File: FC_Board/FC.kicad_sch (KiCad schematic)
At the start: 31 parts, among them J1 Programmer_pins, Q1 PMOS, U1 PIC32MZ2048EFH100-I/PF, U2 LM7805MPX/NOPB, U3 LDL1117S33R

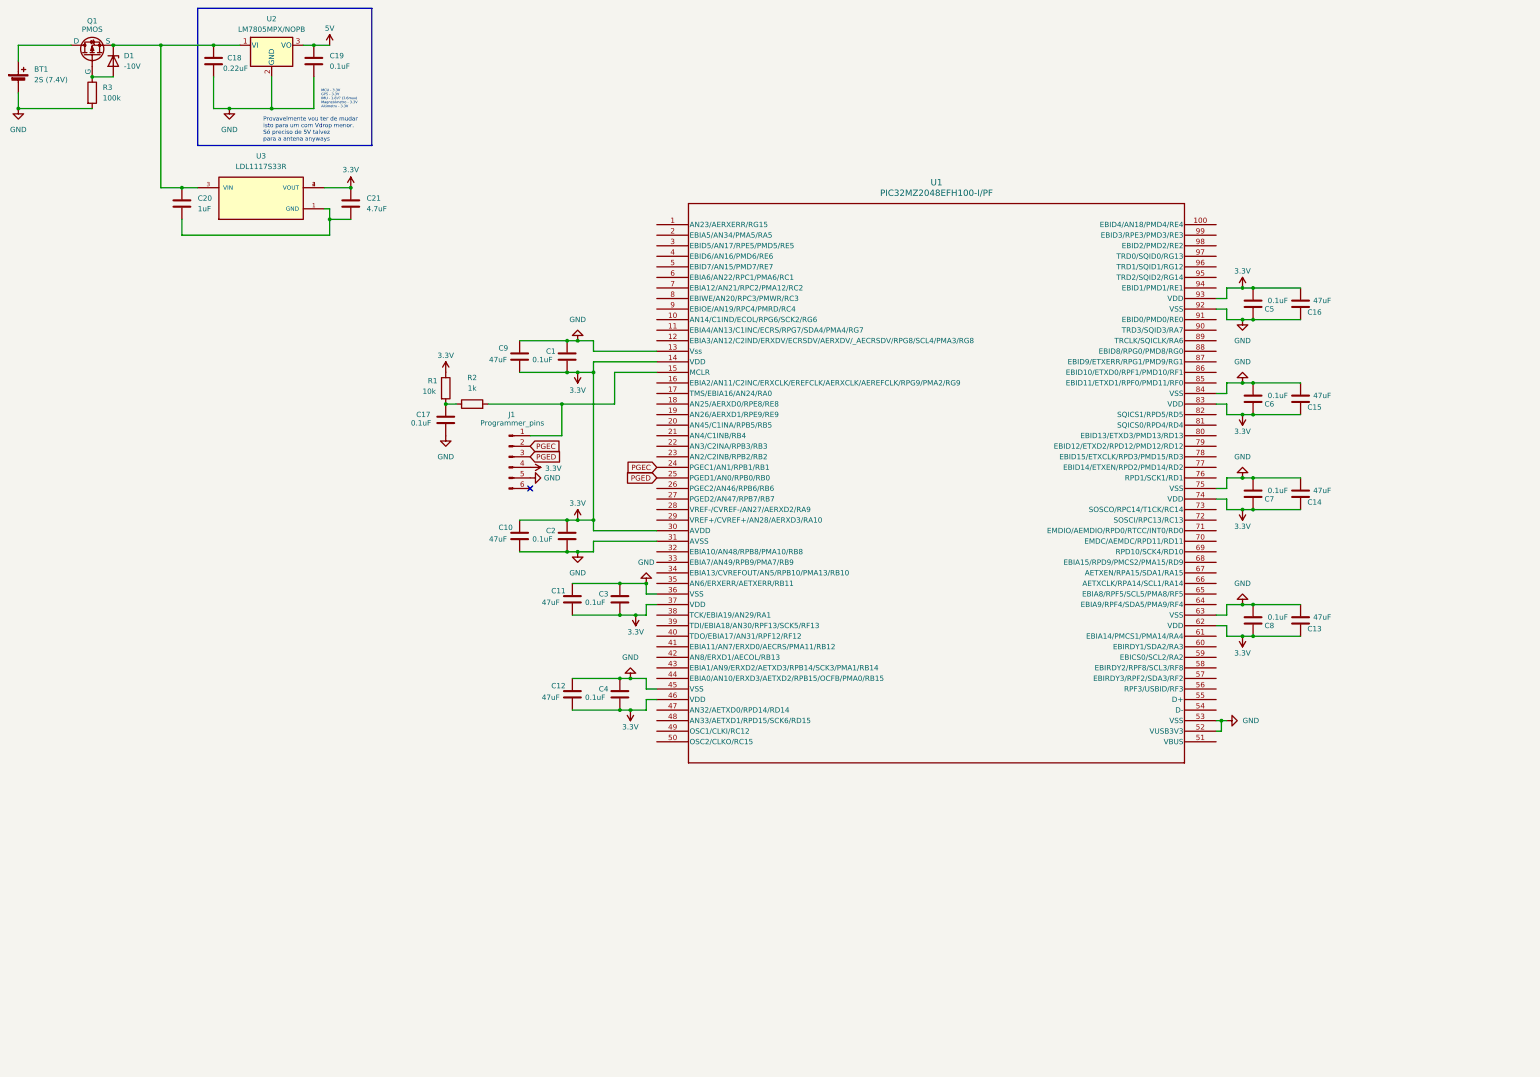
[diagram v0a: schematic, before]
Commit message: Added datasheets and footprints/symbols
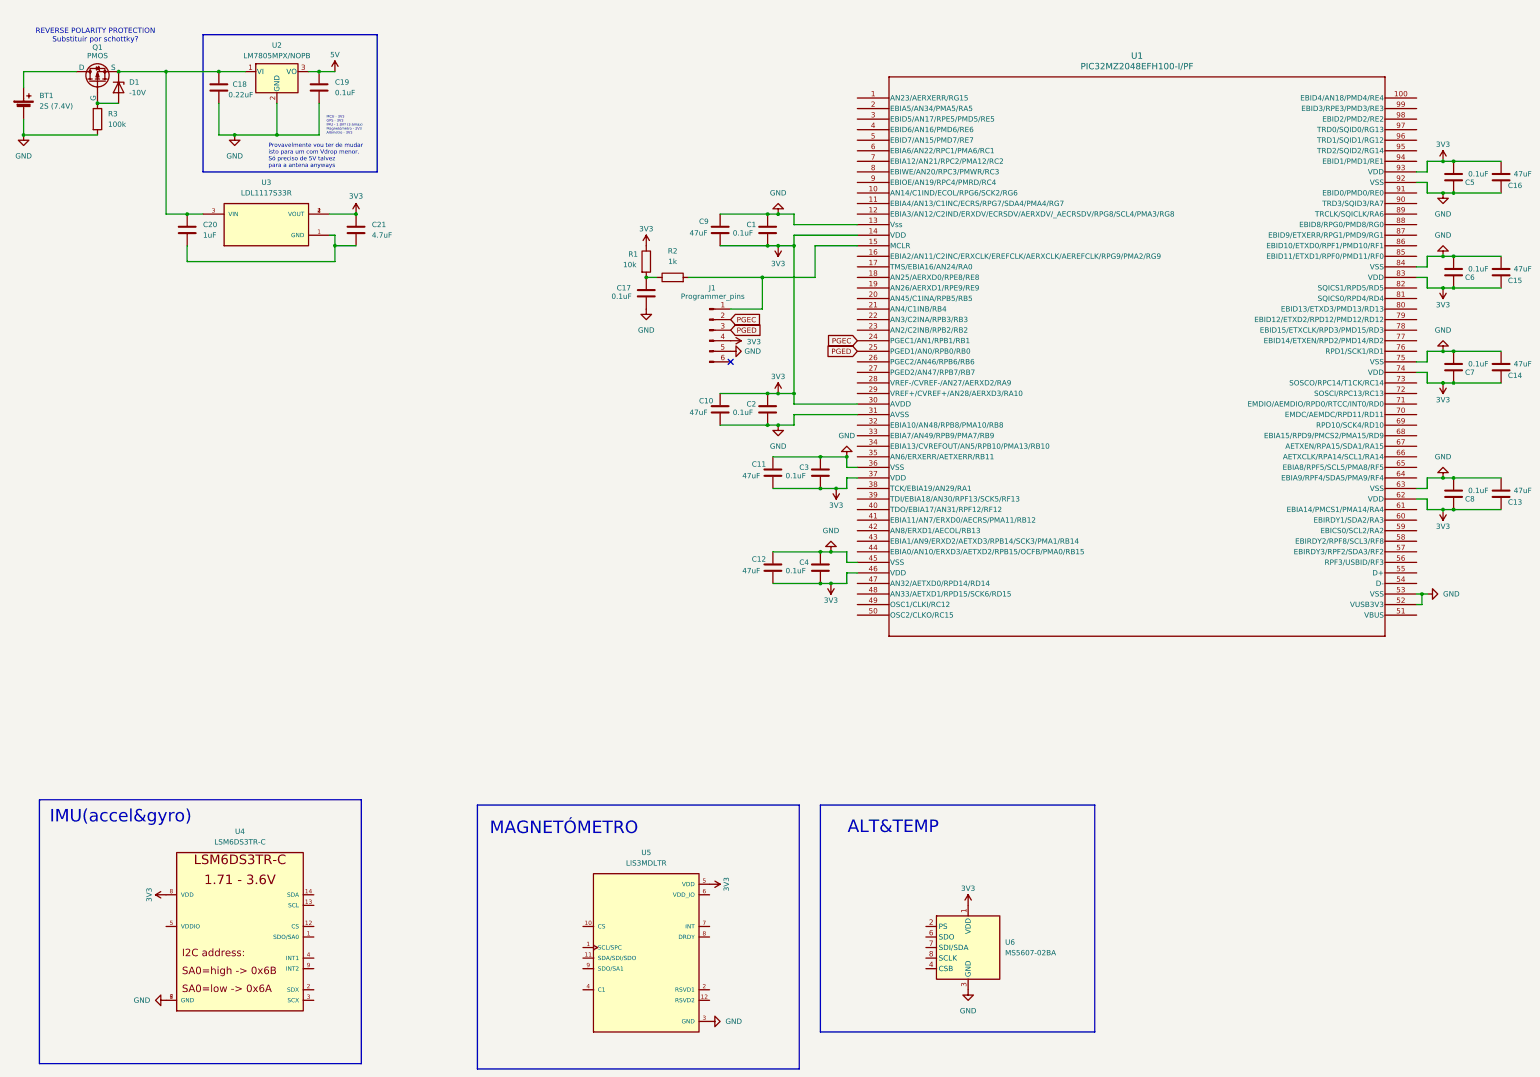
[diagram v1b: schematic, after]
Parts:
- added U4: LSM6DS3TR-C, LSM6DS3TR-C:LGA-14-2.5X3MM, symbol LSM6DS3TR-C:LSM6DS3TR-C
- added U5: LIS3MDLTR, LIS3MDLTR:XDCR_LIS3MDLTR, symbol LIS3MDLTR:LIS3MDLTR
- added U6: MS5607-02BA, Package_LGA:LGA-8_3x5mm_P1.25mm, symbol Sensor_Pressure:MS5607-02BA
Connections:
- net GND: now also U4.6 (GND), U4.7 (GND), U5.3 (GND), U6.3 (GND)
- net 3.3V renamed 3V3
- net 3V3: now also U4.8 (VDD), U5.5 (VDD), U6.1 (VDD)
- new net: U6.4 (CSB), U6.5 (CSB)
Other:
- note added: "ALT&TEMP"
- note added: "IMU(accel&gyro)"
- note added: "MAGNETÓMETRO"
- note added: "MCU - 3V3 GPS - 3V3 IMU - 1.8V? (3.6max) Magnetómetro - 3V3 Altímetro - 3V3"
- note added: "REVERSE POLARITY PROTECTION Substituir por schottky?"
- note removed: "MCU - 3.3V GPS - 3.3V IMU - 1.8V? (3.6max) Magnetómetro - 3.3V Altímetro - 3.3V"
- moved on the sheet: BT1, C1, C10, C11, C12, C13, C14, C15, C16, C17, C18, C19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

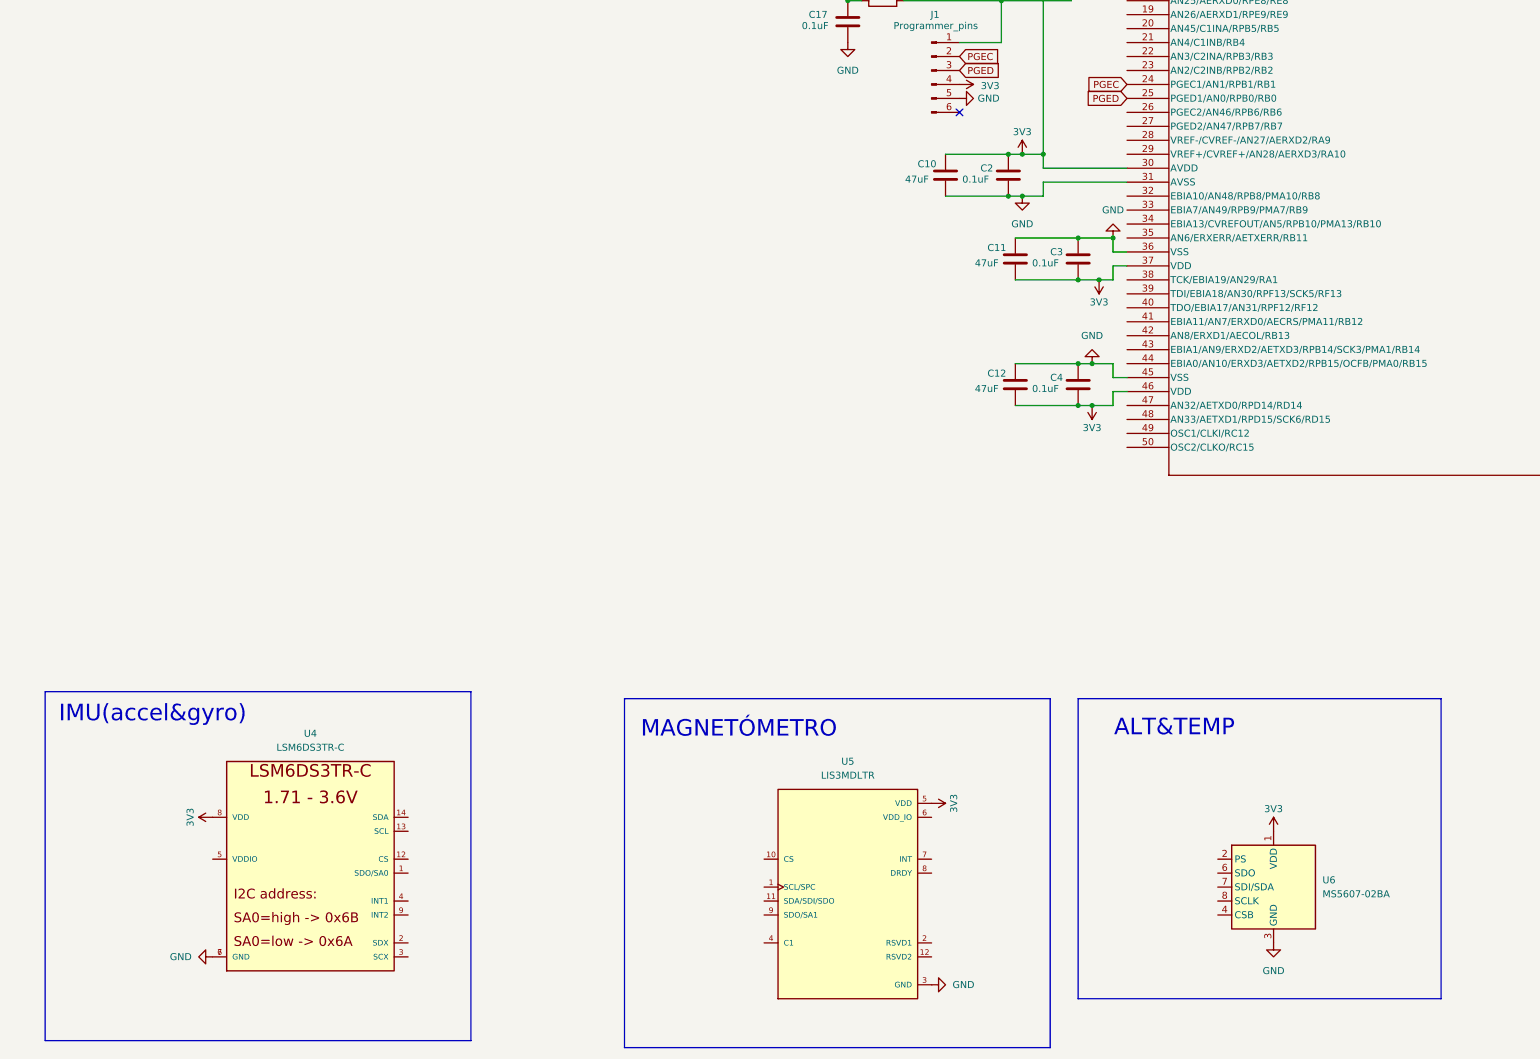
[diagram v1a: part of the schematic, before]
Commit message: Added IC decoupling and basic connections
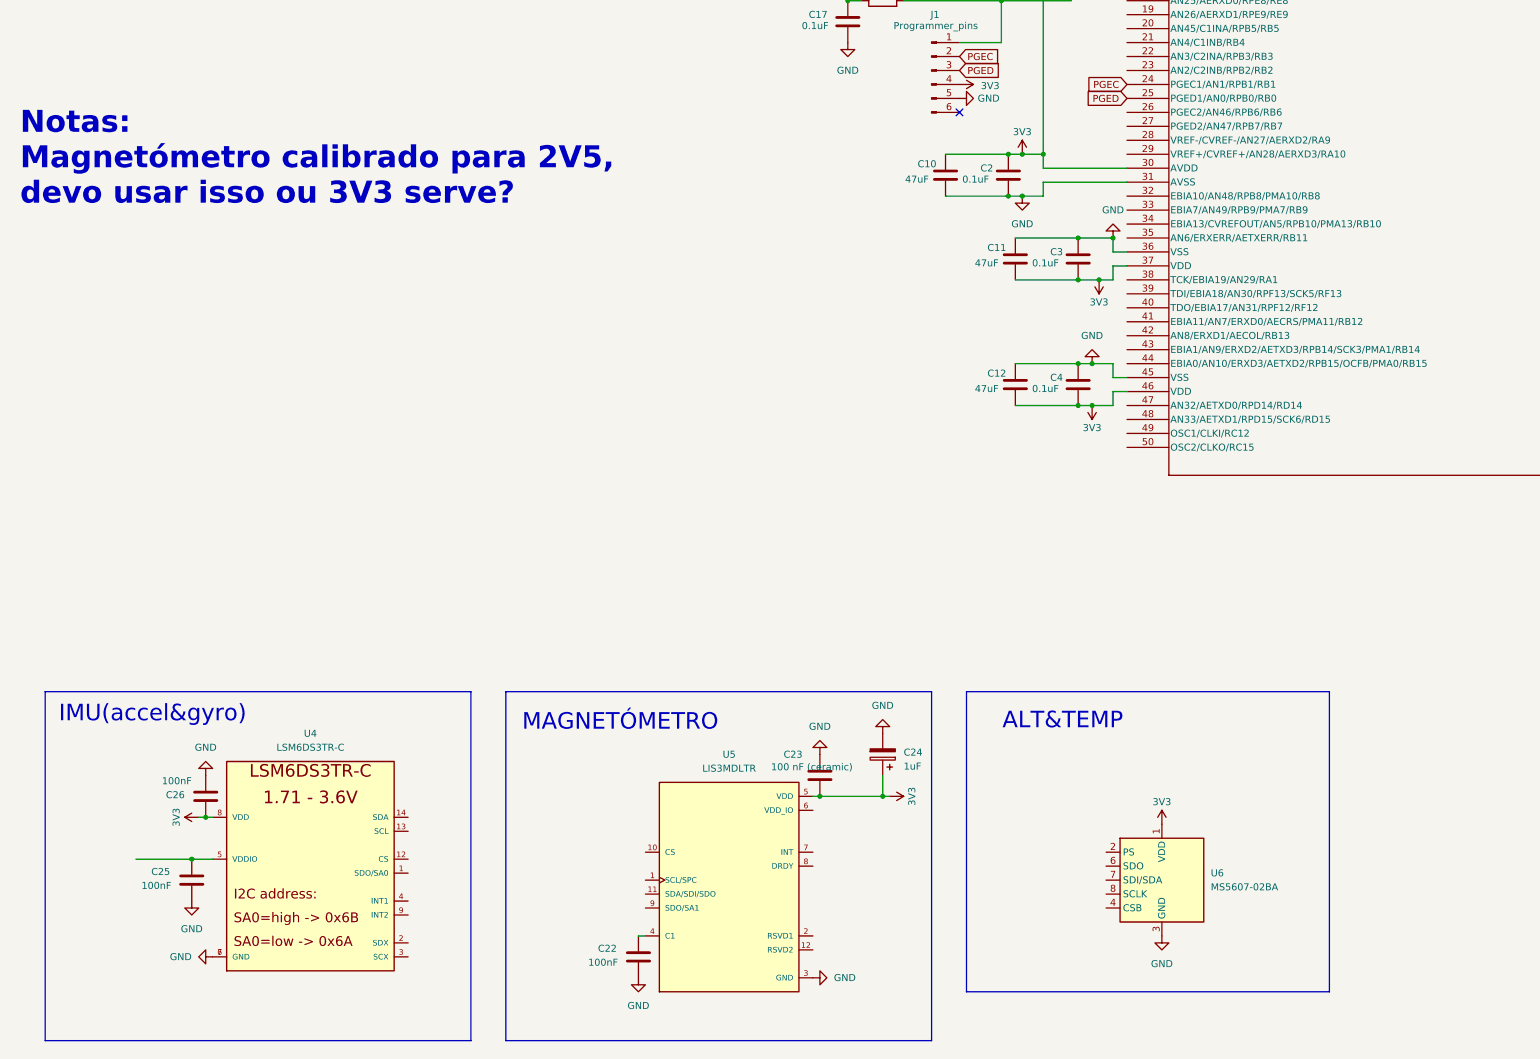
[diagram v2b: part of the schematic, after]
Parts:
- added C22, C25, C26: 100nF, symbol Device:C
- added C23: 100 nF (ceramic), symbol Device:C
- added C24: 1uF, symbol Device:C_Polarized
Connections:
- net 3V3: now also C23.2, C24.1, C26.1
- net GND: now also C22.2, C23.1, C24.2, C25.2, C26.2
- net at U4.5 (VDDIO): now also C25.1
- net at U5.4 (C1): now also C22.1
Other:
- note added: "Notas: Magnetómetro calibrado para 2V5, devo usar isso ou 3V3 serve?"
- moved on the sheet: U5, U6

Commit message: Schematic progress
GPS data logging, Power monitoring and other updates to schematic.
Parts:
- added AE1: Antenna, symbol Device:Antenna
- added BZ1: Buzzer, symbol Device:Buzzer
- added C27: 100 nF (ceramic), symbol Device:C
- added C28, C29, C30: 0.1uF, symbol Device:C
- added C31: C, symbol Device:C
- added D2: LED, symbol Device:LED
- added J2: Pyro1, symbol Connector:Conn_01x02_Pin
- added J3: Pyro2, symbol Connector:Conn_01x02_Pin
- added J4: Pyro3, symbol Connector:Conn_01x02_Pin
- added J5: Pyro4, symbol Connector:Conn_01x02_Pin
- added J6, J7: Conn_01x03, symbol Connector_Generic:Conn_01x03
- added M1, M2, M3, M4: Motor_Servo, symbol Motor:Motor_Servo
- added Q2, Q3, Q4, Q5: NMOS, symbol Simulation_SPICE:NMOS
- added R10, R7, R9: R, symbol Device:R
- added R4, R5, R6: 10k, symbol Device:R
- added R8: R_Shunt, symbol Device:R_Shunt
- added U7: NEO-M8Q, NEO-M8Q:XCVR_NEO-M8Q, symbol NEO-M8Q:NEO-M8Q
- added U8: SST26VF032BT-104I/SM, SOIJ8_SM_MCH, symbol 2025-01-11_19-47-35:SST26VF032BT-104I_SM
- added U9: INA219AxD, Package_SO:SOIC-8_3.9x4.9mm_P1.27mm, symbol Sensor_Energy:INA219AxD
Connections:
- net 3V3: now also C25.1, U4.5 (VDDIO), U5.6 (VDD_IO), C27.2, C28.1, C29.2, C30.2, J6.3 (Pin_3), J7.3 (Pin_3), R4.2, R5.2, R6.2, U7.22 (V_BCKP), U7.23 (VCC), U8.8 (VDD), U9.5 (VS)
- net GND: now also U4.2 (SDX), U4.3 (SCX), U5.12 (RSVD2), U5.2 (RSVD1), BZ1.2 (-), C27.1, C28.2, C29.1, C30.1, J6.1 (Pin_1), J7.1 (Pin_1), M1.3 (-), M2.3 (-), M3.3 (-), M4.3 (-), Q2.3 (S), Q3.3 (S), Q4.3 (S), Q5.3 (S), R7.1, U7.10 (GND), U7.12 (GND), U7.13 (GND), U7.24 (GND), U8.4 (VSS), U9.6 (GND)
- net IMU_SDO: now reaches U4.1 (SDO/SA0)
- net IMU_CS: now reaches U4.12 (CS)
- net IMU_CS: now also R6.1
- net IMU_CLK: now reaches U4.13 (SCL)
- net IMU_SDI: now reaches U4.14 (SDA)
- net at U6.2 (PS): now also J6.2 (Pin_2)
- net ALT_CS: now reaches U6.4 (CSB), U6.5 (CSB)
- net ALT_CS: now also R4.1
- net ALT_SDO: now reaches U6.6 (SDO)
- net ALT_SDI: now reaches U6.7 (SDI/SDA)
- net ALT_CLK: now reaches U6.8 (SCLK)
- net MAG_CLK: now reaches U5.1 (SCL/SPC)
- net MAG_CS: now reaches U5.10 (CS)
- net MAG_CS: now also R5.1
- net MAG_SDI: now reaches U5.11 (SDA/SDI/SDO)
- net MAG_SDO: now reaches U5.9 (SDO/SA1)
- net Battery_VDD: now reaches BT1.1 (+), Q1.1 (D)
- net Battery_VDD: now also J2.1 (Pin_1), J3.1 (Pin_1), J4.1 (Pin_1), J5.1 (Pin_1)
- new net: J2.2 (Pin_2), Q2.1 (D)
- new net: C31.2, R10.1, R8.3
- new net: R10.2, U9.7 (IN-)
- new net: J5.2 (Pin_2), Q5.1 (D)
- new net: R9.2, U9.8 (IN+)
- new net: J3.2 (Pin_2), Q3.1 (D)
- new net: J7.2 (Pin_2), U7.2 (D_SEL)
- new net: J4.2 (Pin_2), Q4.1 (D)
- new net: C31.1, R8.2, R9.1
- new net: D2.1 (K), R7.2
- new net: AE1.1 (A), U7.11 (RF_IN)
- new net Buzzer_pin: BZ1.1 (+), D2.2 (A)
- new net FLASH_CLK: U8.6 (SCK)
- new net FLASH_EN: U8.1 (CE#)
- new net GPS_CLK: U7.19 (SCL/SPI_CLK)
- new net GPS_CS: U7.18 (SDA/SPI_CS_N)
- new net GPS_INT: U7.4 (EXTINT)
- new net GPS_RESET: U7.8 (RESET_N)
- new net GPS_RXD: U7.21 (RXD/SPI_MOSI)
- new net GPS_TXD: U7.20 (TXD/SPI_MISO)
- new net PWR_SDA: U9.3 (SDA)
- new net PWR_SDL: U9.4 (SCL)
- new net Pyro_channel1: Q2.2 (G)
- new net Pyro_channel2: Q3.2 (G)
- new net Pyro_channel3: Q4.2 (G)
- new net Pyro_channel4: Q5.2 (G)
- new net SERVO_+: M1.2 (+), M2.2 (+), M3.2 (+), M4.2 (+)
- new net SERVO_1: M1.1 (PWM)
- new net SERVO_2: M2.1 (PWM)
- new net SERVO_3: M3.1 (PWM)
- new net SERVO_4: M4.1 (PWM)
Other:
- note added: "Active antenna only"
- note added: "Buzzer"
- note added: "Confirmar mais tarde ligações a pinos A0/A1"
- note added: "Convém confirmar se PIC consegue dar drive do buzzer e led simultaneamente, talvez fosse boa ideia usar open drain type config"
- note added: "De preferência ter este sinal num canal separado ao invés dum barramento. (ADC sensível / Recomendado no datasheet)"
- note added: "GPS"
- note added: "GPS FLASH DATA LOGGING"
- note added: "I2C"
- note added: "LNA EN (caso use LNA externo)"
- note added: "Ler datasheet para determinar valor do shunt"
- note added: "Ligar USB para dar debug ao GPS?"
- note added: "Ligar a GPIO's"
- note added: "MCU"
- note added: "Marcar na PCB qual é o pin1"
- note added: "Notas: - 5V necessário? - Calcular Pull resistors do SPI - Conectores para ler flash memory - Adicionar possibilidade de ter resistências série para linhas de transmissão - Interrupts? - Pull-ups nos clocks? (I2C) - Sou capaz de precisar de mais reguladores de tensão para ter corrente suficiente - Ligar flash memory ao GPS"
- note added: "POWER MONITORING"
- note added: "Potencial filtragem. Tenho de confirmar se será necessário mas penso que não, o mais provável é deixar na PCB e logo decidir se meto componentes ou só dou bypass."
- note added: "Pyro 1"
- note added: "Pyro 2"
- note added: "Pyro 3"
- note added: "Pyro 4"
- note added: "SERVOS"
- note added: "SPI"
- note added: "Tenho de decidir qual das linhas quero monitorizar. Overall power?PIC?... Suponho que nada me impede ter vários ICs a ver linhas diferentes mas parece-me excessivo."
- note added: "Timepulse (probably no connect)"
- note added: "Transistores chegam a abrir completamente se a tensão da bateria fôr superior à tensão aplicada pelo PIC na gate?"
- note added: "UART/DDC"
- note added: "VDD_USB ligado a GND caso não vá usar o USB"
- note added: "Vale a pena adicionar um conector para ligar uma bateria de backup? (3V3)"
- note removed: "Notas: Magnetómetro calibrado para 2V5, devo usar isso ou 3V3 serve?"
- moved on the sheet: BT1, C1, C10, C11, C12, C13, C14, C15, C16, C17, C18, C19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

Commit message: Added SD card and some other basic stuff
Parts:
- added C32: 0.1uF, symbol Device:C
- added D3: LED, symbol Device:LED
- added F1: Fuse, symbol Device:Fuse
- added J8: MEM2090-00-145-00-A_REVA, MEM2090-00-145-00-A_REVA:GCT_MEM2090-00-145-00-A_REVA, symbol MEM2090-00-145-00-A_REVA SD:MEM2090-00-145-00-A_REVA
- added R11: R, symbol Device:R
- added R12: 10k, symbol Device:R
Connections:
- net 3V3: now also C32.1, J8.P4 (VDD), R12.1
- net Battery_VDD: now also F1.1; no longer Q1.1 (D)
- net GND: now also C32.2, D3.1 (K), J8.G1 (GND), J8.G2 (GND), J8.G3 (GND), J8.G4 (GND), J8.G5 (GND), J8.G6 (GND), J8.P6 (VSS)
- net at U7.3 (TIMEPULSE): now also R11.2
- new net: F1.2, Q1.1 (D)
- new net: D3.2 (A), R11.1
- new net SD_CLK: J8.P5 (CLK)
- new net SD_CMD: J8.P3 (CMD)
- new net SD_D0: J8.P7 (DAT0)
- new net SD_D1: J8.P8 (DAT1)
- new net SD_D2: J8.P1 (DAT2)
- new net SD_D3: J8.P2 (CD/DAT3)
- new net SD_IN#: J8.SW (SWITCH), R12.2
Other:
- note added: "Adicionar interface leitura. USB maybe? Bué bulky idk..."
- note added: "Como é que este CMD funciona? Sequer preciso em modo SPI?"
- note added: "Notas: - 5V necessário? - Calcular Pull resistors do SPI - Conectores para ler flash memory - Adicionar possibilidade de ter resistências série para linhas de transmissão - Interrupts? - Pull-ups nos clocks? (I2C) - Sou capaz de precisar de mais reguladores de tensão para ter corrente suficiente - Ligar flash memory ao GPS - Antena activa ou passiva (GPS)? - Verificar valores de decouplers"
- note added: "SD CARD"
- note removed: "Notas: - 5V necessário? - Calcular Pull resistors do SPI - Conectores para ler flash memory - Adicionar possibilidade de ter resistências série para linhas de transmissão - Interrupts? - Pull-ups nos clocks? (I2C) - Sou capaz de precisar de mais reguladores de tensão para ter corrente suficiente - Ligar flash memory ao GPS"
- note removed: "Timepulse (probably no connect)"
